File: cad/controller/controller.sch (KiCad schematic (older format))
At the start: 64 parts, among them J1 RJ45_jack_POE, J2 Barrel_Jack, SW1 SW_Push, U1 NCP1117-5.0_SOT223, U2 NCP1117-3.3_SOT223, U3 CAT811STBI-GT3, U4 W5500, Y1 25MHz

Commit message: controller placement in progress
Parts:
- Y1: footprint Crystal:Crystal_SMD_HC49-SD_HandSoldering -> Crystal:Crystal_SMD_HC49-SD
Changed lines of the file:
@@
 F 0 "Y1" V 2404 4181 50  0000 L CNN
 F 1 "25MHz" V 2495 4181 50  0000 L CNN
-F 2 "Crystal:Crystal_SMD_HC49-SD_HandSoldering" H 2450 4050 50  0001 C CNN
+F 2 "Crystal:Crystal_SMD_HC49-SD" H 2450 4050 50  0001 C CNN
 F 3 "~" H 2450 4050 50  0001 C CNN
 	1    2450 4050

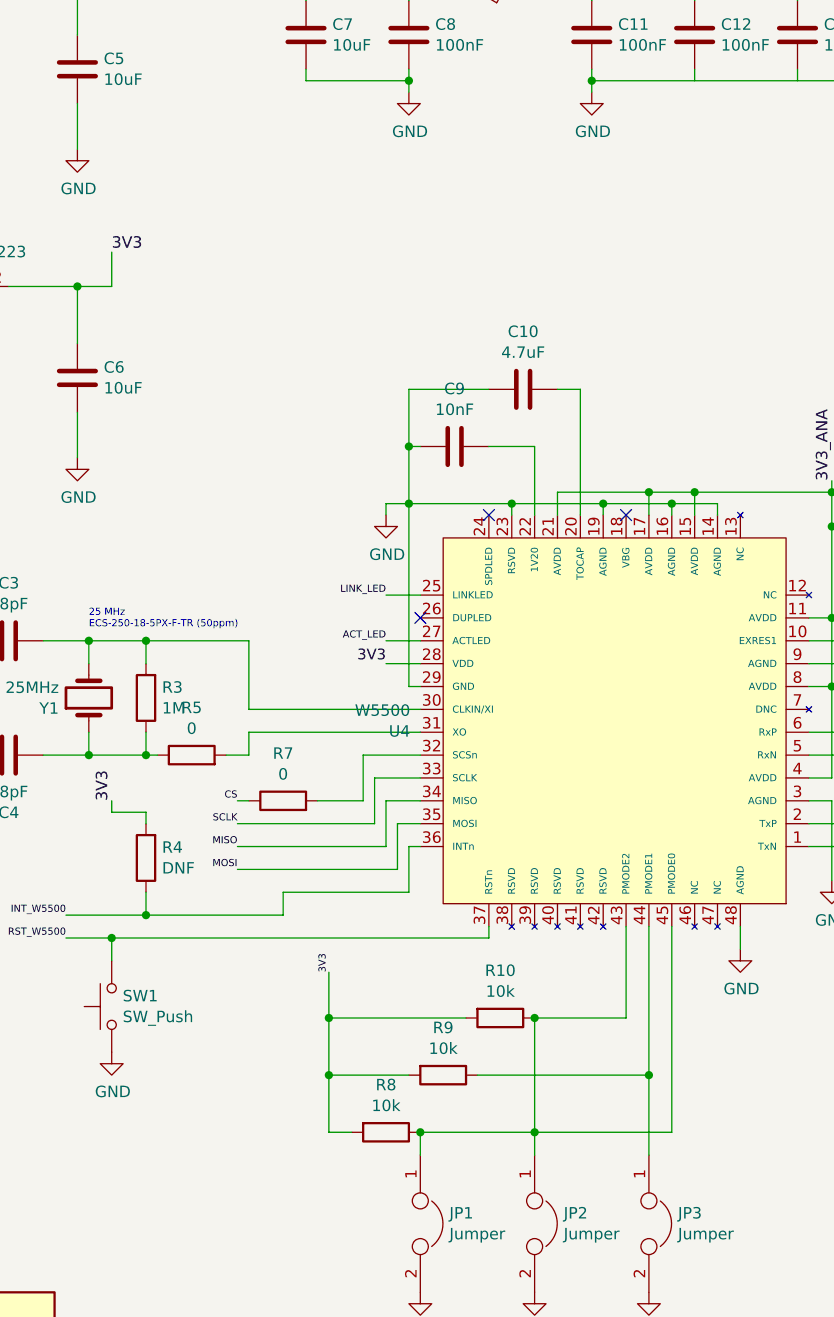
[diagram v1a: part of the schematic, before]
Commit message: Continued controller board placement
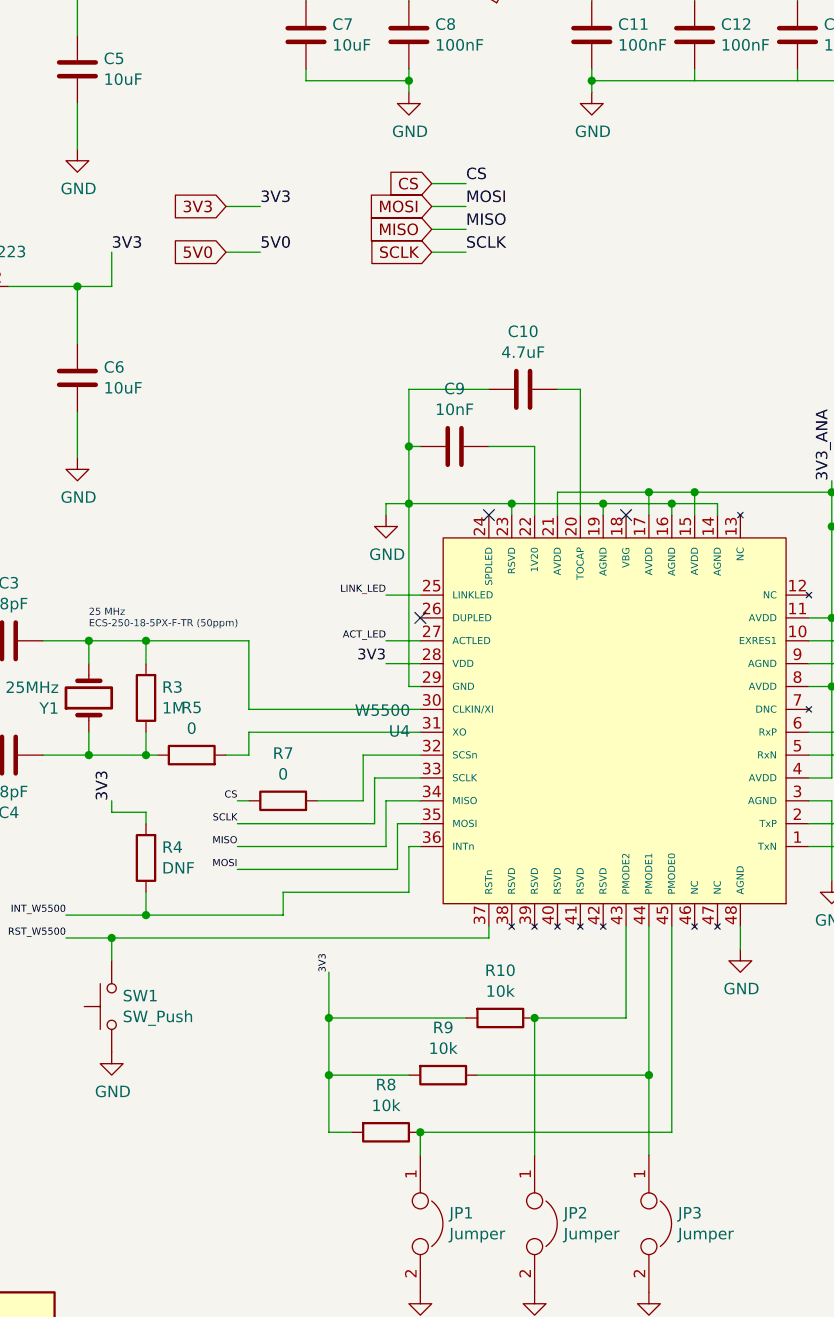
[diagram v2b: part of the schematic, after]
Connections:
- net at JP2.1, R10.1, U4.43 (PMODE2): no longer JP1.1, R8.1, U4.45 (PMODE0)
- new net: JP1.1, R8.1, U4.45 (PMODE0)
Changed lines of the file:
@@
 	2550 2250 2550 2100
 Connection ~ 2400 2250
-Text Label 2550 2100 0    50   ~ 0
-3V3
 $Comp
 L power:GND #PWR04
@@
 Wire Wire Line
 	4650 900  4650 1000
-Text Label 3250 900  2    50   ~ 0
-3V3
 Wire Wire Line
 	4400 900  4650 900
@@
 $EndComp
 Wire Wire Line
-	3900 5950 4400 5950
-Wire Wire Line
 	3900 6050 3900 5950
 Connection ~ 3900 5950
@@
 Wire Wire Line
 	4400 5450 4800 5450
-Wire Wire Line
-	4400 5950 4400 5450
-Connection ~ 4400 5450
 Wire Wire Line
 	7300 4350 7300 4750
@@
 Wire Wire Line
 	4900 5700 4900 6050
-Connection ~ 4400 5950
-Wire Wire Line
-	4400 5950 5000 5950
 Wire Wire Line
 	4800 5450 4800 5050
-Wire Wire Line
-	4400 6050 4400 5950
 Wire Wire Line
 	3500 5450 3500 5700
@@
 Wire Wire Line
 	9100 6100 8950 6100
+Wire Wire Line
+	3900 5950 5000 5950
+Wire Wire Line
+	4400 5450 4400 6050
+Connection ~ 4400 5450
+Text Label 3250 900  2    50   ~ 0
+3V3
+Text GLabel 3050 1900 0    50   Input ~ 0
+3V3
+Text Label 2550 2100 0    50   ~ 0
+3V3
+Text Label 3200 1900 0    50   ~ 0
+3V3
+Wire Wire Line
+	3050 1900 3200 1900
+Text GLabel 3050 2100 0    50   Input ~ 0
+5V0
+Text Label 3200 2100 0    50   ~ 0
+5V0
+Wire Wire Line
+	3050 2100 3200 2100
+Text Label 4100 2100 0    50   ~ 0
+SCLK
+Text Label 4100 2000 0    50   ~ 0
+MISO
+Text Label 4100 1900 0    50   ~ 0
+MOSI
+Text Label 4100 1800 0    50   ~ 0
+CS
+Text GLabel 3950 1800 0    50   Input ~ 0
+CS
+Text GLabel 3950 1900 0    50   Input ~ 0
+MOSI
+Text GLabel 3950 2000 0    50   Input ~ 0
+MISO
+Text GLabel 3950 2100 0    50   Input ~ 0
+SCLK
+Wire Wire Line
+	3950 1800 4100 1800
+Wire Wire Line
+	3950 1900 4100 1900
+Wire Wire Line
+	3950 2000 4100 2000
+Wire Wire Line
+	3950 2100 4100 2100
 $EndSCHEMATC

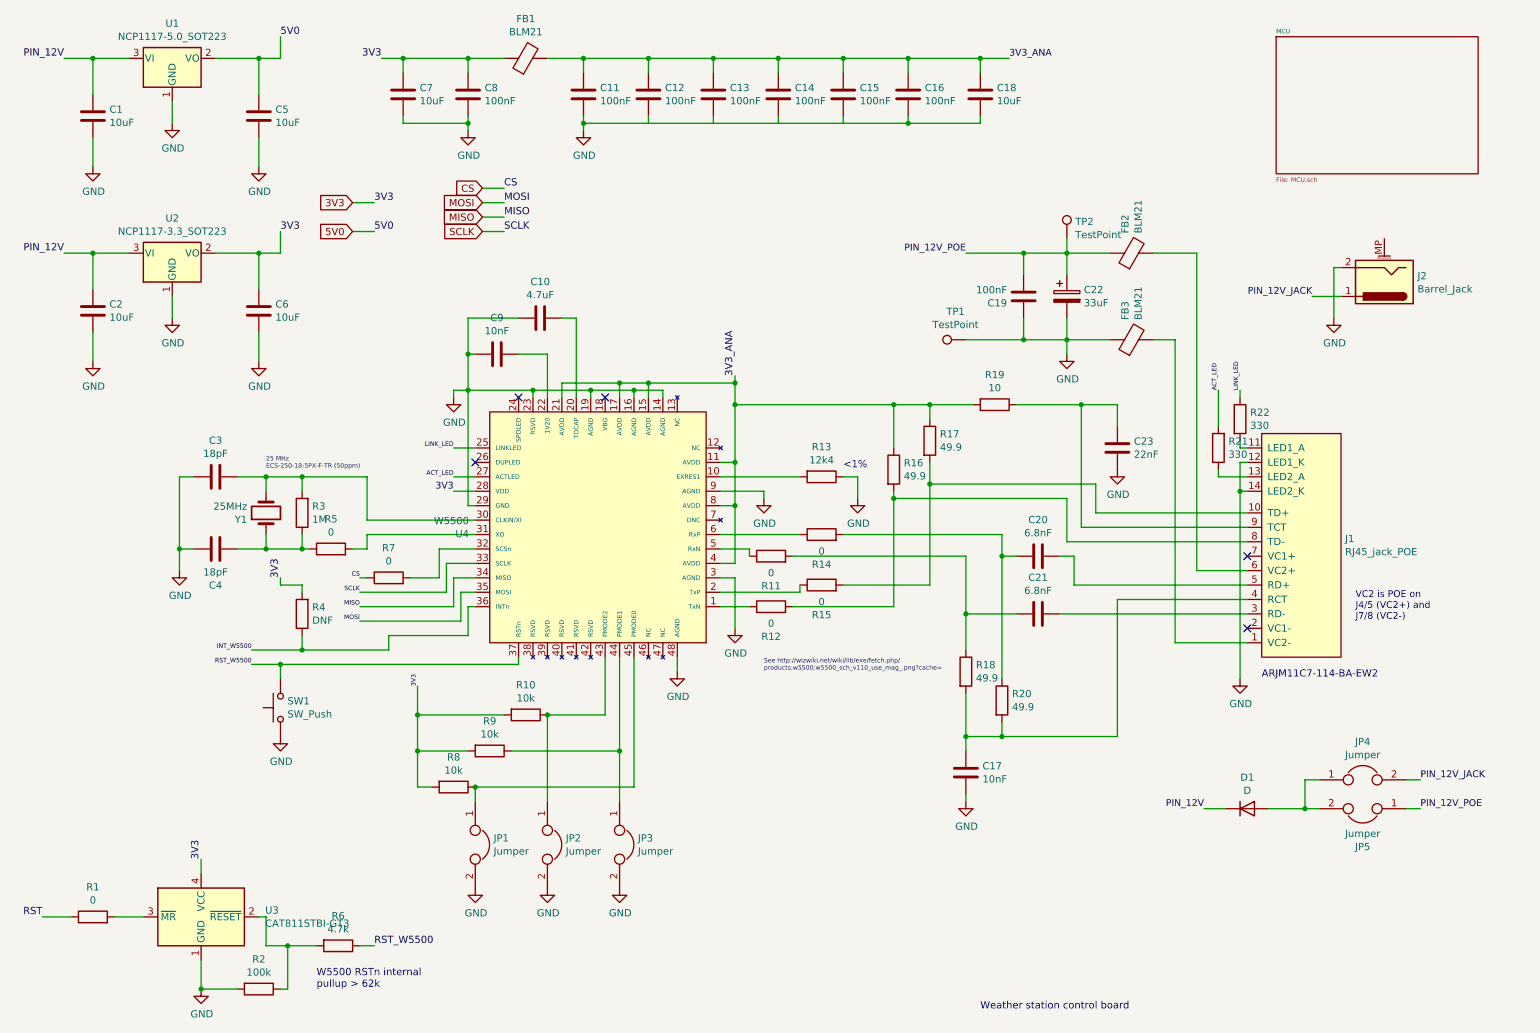
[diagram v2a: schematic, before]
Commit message: Finished placement of controller
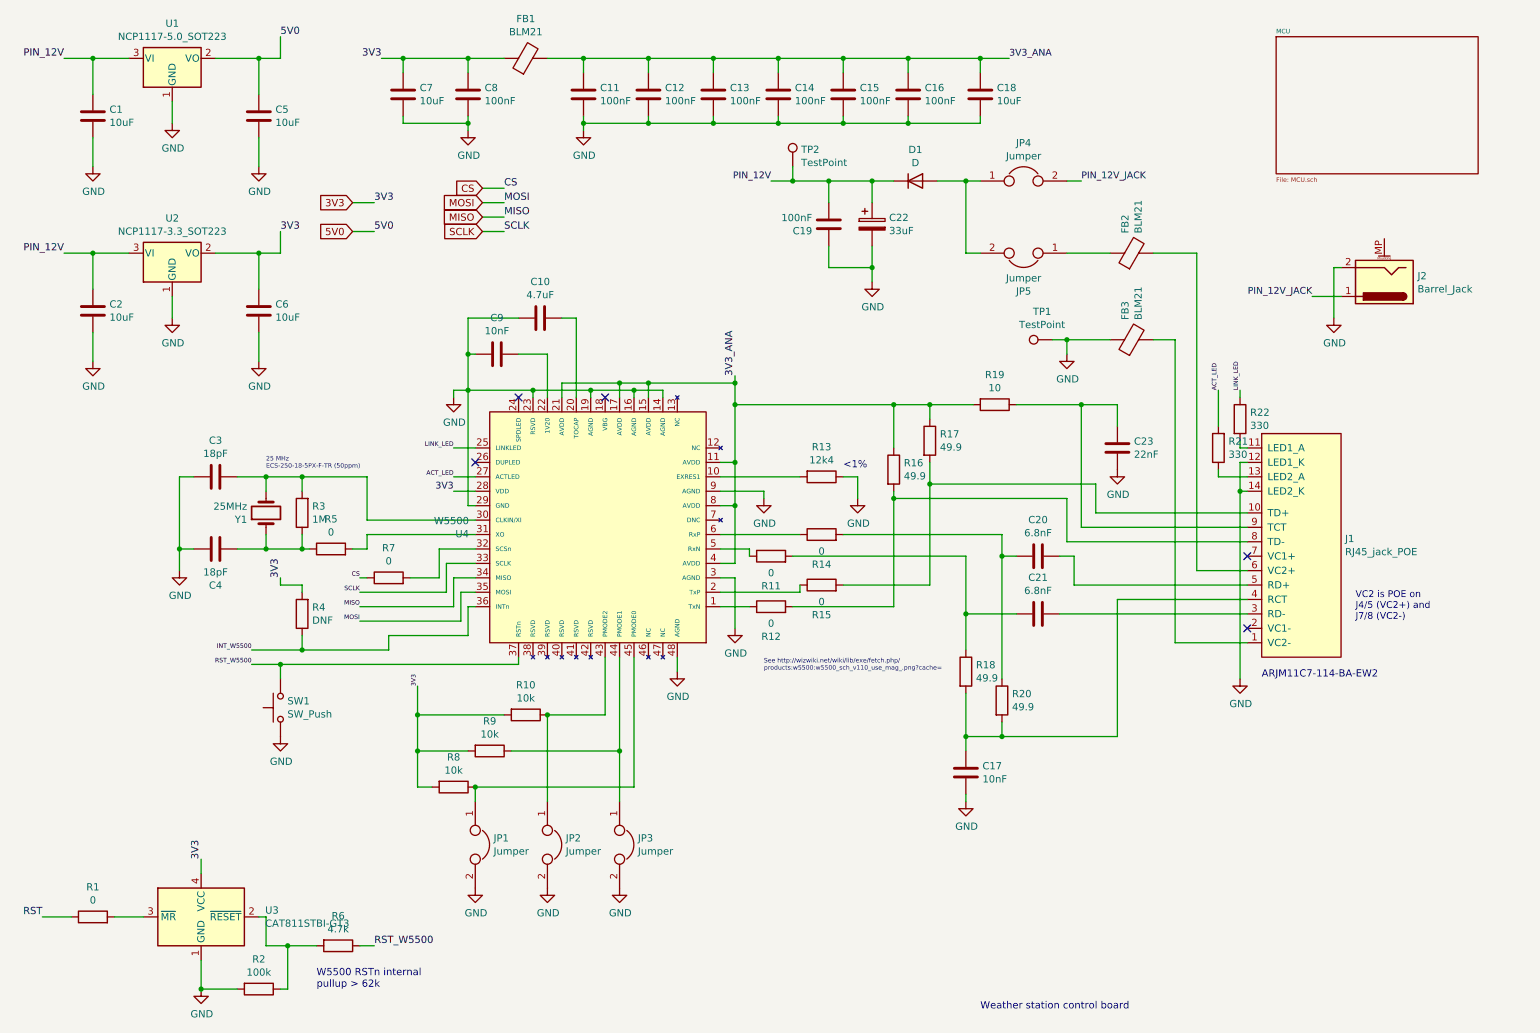
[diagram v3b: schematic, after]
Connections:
- net GND: now also C12.1, C13.1, C14.1, C15.1
- net PIN_12V: now also C19.1, C22.1, TP2.1
- removed net PIN_12V_POE: C19.1, C22.1, FB2.1, JP5.1, TP2.1
- new net: FB2.1, JP5.1
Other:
- moved on the sheet: C19, C22, D1, JP4, JP5, TP1, TP2
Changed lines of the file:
@@
 Text Notes 10000 4800 0    47   ~ 0
 VC2 is POE on\nJ4/5 (VC2+) and\nJ7/8 (VC2-)
-Text Label 7300 2250 2    47   ~ 0
-PIN_12V_POE
 NoConn ~ 9250 4350
 NoConn ~ 9250 4850
@@
 L Device:Jumper JP5
 U 1 1 624A0154
-P 10050 6100
-F 0 "JP5" H 10050 6364 50  0000 C CNN
-F 1 "Jumper" H 10050 6273 50  0000 C CNN
-F 2 "Connector_PinSocket_2.54mm:PinSocket_1x02_P2.54mm_Vertical" H 10050 6100 50  0001 C CNN
-F 3 "~" H 10050 6100 50  0001 C CNN
-	1    10050 6100
+P 7700 2250
+F 0 "JP5" H 7700 2514 50  0000 C CNN
+F 1 "Jumper" H 7700 2423 50  0000 C CNN
+F 2 "Connector_PinSocket_2.54mm:PinSocket_1x02_P2.54mm_Vertical" H 7700 2250 50  0001 C CNN
+F 3 "~" H 7700 2250 50  0001 C CNN
+	1    7700 2250
 	-1   0    0    1
 $EndComp
@@
 L Device:Jumper JP4
 U 1 1 624A141E
-P 10050 5900
-F 0 "JP4" H 10050 6164 50  0000 C CNN
-F 1 "Jumper" H 10050 6073 50  0000 C CNN
-F 2 "Connector_PinSocket_2.54mm:PinSocket_1x02_P2.54mm_Vertical" H 10050 5900 50  0001 C CNN
-F 3 "~" H 10050 5900 50  0001 C CNN
-	1    10050 5900
-	1    0    0    -1
-$EndComp
-Wire Wire Line
-	9750 5900 9650 5900
-Wire Wire Line
-	9650 5900 9650 6100
-Wire Wire Line
-	9750 6100 9650 6100
-Connection ~ 9650 6100
-Wire Wire Line
-	10350 6100 10450 6100
-Wire Wire Line
-	10350 5900 10450 5900
-Text Label 10450 6100 0    47   ~ 0
-PIN_12V_POE
-Text Label 10450 5900 0    47   ~ 0
+P 7700 1750
+F 0 "JP4" H 7700 2014 50  0000 C CNN
+F 1 "Jumper" H 7700 1923 50  0000 C CNN
+F 2 "Connector_PinSocket_2.54mm:PinSocket_1x02_P2.54mm_Vertical" H 7700 1750 50  0001 C CNN
+F 3 "~" H 7700 1750 50  0001 C CNN
+	1    7700 1750
+	1    0    0    -1
+$EndComp
+Wire Wire Line
+	7400 2250 7300 2250
+Wire Wire Line
+	8000 1750 8100 1750
+Text Label 8100 1750 0    47   ~ 0
 PIN_12V_JACK
-Text Label 8950 6100 2    47   ~ 0
+Text Label 5950 1750 2    47   ~ 0
 PIN_12V
 Wire Wire Line
@@
 Wire Wire Line
 	8600 2850 8750 2850
-Wire Wire Line
-	8000 2250 8300 2250
 $Comp
 L power:GND #PWR021
@@
 	1    0    0    -1
 $EndComp
-Connection ~ 8000 2250
 Wire Wire Line
 	8000 2850 8000 2950
-Connection ~ 8000 2850
 $Comp
 L Connector:TestPoint TP2
 U 1 1 62BD0C2D
-P 8000 2150
-F 0 "TP2" H 8058 2268 50  0000 L CNN
-F 1 "TestPoint" H 8058 2177 50  0000 L CNN
-F 2 "TestPoint:TestPoint_Pad_2.5x2.5mm" H 8200 2150 50  0001 C CNN
-F 3 "~" H 8200 2150 50  0001 C CNN
-	1    8000 2150
-	1    0    0    -1
-$EndComp
-$Comp
-L Connector:TestPoint TP1
-U 1 1 62BD24C9
-P 7300 2850
-F 0 "TP1" V 7495 2922 50  0000 C CNN
-F 1 "TestPoint" V 7404 2922 50  0000 C CNN
-F 2 "TestPoint:TestPoint_Pad_2.5x2.5mm" H 7500 2850 50  0001 C CNN
-F 3 "~" H 7500 2850 50  0001 C CNN
-	1    7300 2850
-	0    -1   -1   0
+P 6100 1650
+F 0 "TP2" H 6158 1768 50  0000 L CNN
+F 1 "TestPoint" H 6158 1677 50  0000 L CNN
+F 2 "TestPoint:TestPoint_Pad_2.5x2.5mm" H 6300 1650 50  0001 C CNN
+F 3 "~" H 6300 1650 50  0001 C CNN
+	1    6100 1650
+	1    0    0    -1
 $EndComp
 Wire Wire Line
 	8300 2850 8000 2850
-Wire Wire Line
-	8000 2250 8000 2150
 $Comp
 L Device:C C8
@@
 Wire Wire Line
 	3850 900  3850 1000
-Wire Wire Line
-	4650 1300 4650 1350
-Wire Wire Line
-	4650 1350 6900 1350
 $Comp
 L Device:C C12
@@
 	-1   0    0    1
 $EndComp
-Wire Wire Line
-	5100 1300 5100 1350
 $Comp
 L Device:C C13
@@
 	-1   0    0    1
 $EndComp
-Wire Wire Line
-	5550 1300 5550 1350
 $Comp
 L Device:C C14
@@
 	-1   0    0    1
 $EndComp
-Wire Wire Line
-	6000 1300 6000 1350
 $Comp
 L Device:C C15
@@
 	-1   0    0    1
 $EndComp
-Wire Wire Line
-	6450 1300 6450 1350
 $Comp
 L Device:C C16
@@
 Wire Wire Line
 	6900 1350 7400 1350
-Connection ~ 6900 1350
-Wire Wire Line
-	4650 1350 4650 1400
-Connection ~ 4650 1350
 Connection ~ 3850 1350
 $Comp
 L Device:CP C22
 U 1 1 6313C837
-P 8000 2550
-F 0 "C22" H 8118 2596 50  0000 L CNN
-F 1 "33uF" H 8118 2505 50  0000 L CNN
-F 2 "Capacitor_THT:CP_Radial_D4.0mm_P2.00mm" H 8038 2400 50  0001 C CNN
-F 3 "~" H 8000 2550 50  0001 C CNN
-	1    8000 2550
-	1    0    0    -1
-$EndComp
-Wire Wire Line
-	8000 2250 8000 2400
-Wire Wire Line
-	8000 2700 8000 2850
+P 6650 2050
+F 0 "C22" H 6768 2096 50  0000 L CNN
+F 1 "33uF" H 6768 2005 50  0000 L CNN
+F 2 "Capacitor_THT:CP_Radial_D4.0mm_P2.00mm" H 6688 1900 50  0001 C CNN
+F 3 "~" H 6650 2050 50  0001 C CNN
+	1    6650 2050
+	1    0    0    -1
+$EndComp
+Wire Wire Line
+	6650 1750 6650 1900
+Wire Wire Line
+	6650 2200 6650 2350
 $Comp
 L Device:C C19
 U 1 1 62415D4C
-P 7700 2550
-F 0 "C19" H 7585 2504 50  0000 R CNN
-F 1 "100nF" H 7585 2595 50  0000 R CNN
-F 2 "Capacitor_SMD:C_0603_1608Metric" H 7738 2400 50  0001 C CNN
-F 3 "~" H 7700 2550 50  0001 C CNN
-	1    7700 2550
-	1    0    0    -1
-$EndComp
-Wire Wire Line
-	7700 2250 7700 2400
-Wire Wire Line
-	7700 2250 8000 2250
-Wire Wire Line
-	7700 2850 7700 2700
-Wire Wire Line
-	7700 2850 8000 2850
-Wire Wire Line
-	7700 2850 7300 2850
-Connection ~ 7700 2850
-Wire Wire Line
-	7700 2250 7300 2250
-Connection ~ 7700 2250
+P 6350 2050
+F 0 "C19" H 6235 2004 50  0000 R CNN
+F 1 "100nF" H 6235 2095 50  0000 R CNN
+F 2 "Capacitor_SMD:C_0603_1608Metric" H 6388 1900 50  0001 C CNN
+F 3 "~" H 6350 2050 50  0001 C CNN
+	1    6350 2050
+	1    0    0    -1
+$EndComp
+Wire Wire Line
+	6350 1750 6350 1900
+Wire Wire Line
+	6350 2350 6350 2200
 $Comp
 L Device:C C7
@@
 L Device:D D1
 U 1 1 62437589
-P 9250 6100
-F 0 "D1" H 9250 6317 50  0000 C CNN
-F 1 "D" H 9250 6226 50  0000 C CNN
-F 2 "Diode_THT:D_DO-41_SOD81_P7.62mm_Horizontal" H 9250 6100 50  0001 C CNN
-F 3 "~" H 9250 6100 50  0001 C CNN
-	1    9250 6100
-	1    0    0    -1
-$EndComp
-Wire Wire Line
-	9400 6100 9650 6100
-Wire Wire Line
-	9100 6100 8950 6100
+P 6950 1750
+F 0 "D1" H 6950 1967 50  0000 C CNN
+F 1 "D" H 6950 1876 50  0000 C CNN
+F 2 "Diode_THT:D_DO-41_SOD81_P7.62mm_Horizontal" H 6950 1750 50  0001 C CNN
+F 3 "~" H 6950 1750 50  0001 C CNN
+	1    6950 1750
+	1    0    0    -1
+$EndComp
+Wire Wire Line
+	6800 1750 6650 1750
 Wire Wire Line
 	3900 5950 5000 5950
@@
 Wire Wire Line
 	3950 2100 4100 2100
+Wire Wire Line
+	4650 1300 4650 1350
+Wire Wire Line
+	6450 1300 6450 1350
+Wire Wire Line
+	6450 1350 6900 1350
+Connection ~ 6900 1350
+Wire Wire Line
+	6000 1300 6000 1350
+Wire Wire Line
+	6000 1350 6450 1350
+Connection ~ 6450 1350
+Wire Wire Line
+	5550 1300 5550 1350
+Wire Wire Line
+	5550 1350 6000 1350
+Connection ~ 6000 1350
+Wire Wire Line
+	5100 1300 5100 1350
+Wire Wire Line
+	5100 1350 5550 1350
+Connection ~ 5550 1350
+Wire Wire Line
+	5100 1350 4650 1350
+Connection ~ 5100 1350
+Connection ~ 4650 1350
+Wire Wire Line
+	4650 1350 4650 1400
+Wire Wire Line
+	7100 1750 7300 1750
+$Comp
+L Connector:TestPoint TP1
+U 1 1 62BD24C9
+P 7900 2850
+F 0 "TP1" V 8095 2922 50  0000 C CNN
+F 1 "TestPoint" V 8004 2922 50  0000 C CNN
+F 2 "TestPoint:TestPoint_Pad_2.5x2.5mm" H 8100 2850 50  0001 C CNN
+F 3 "~" H 8100 2850 50  0001 C CNN
+	1    7900 2850
+	0    -1   -1   0
+$EndComp
+Wire Wire Line
+	8000 2850 7900 2850
+Connection ~ 8000 2850
+Wire Wire Line
+	7300 1750 7400 1750
+Wire Wire Line
+	8000 2250 8300 2250
+Connection ~ 7300 1750
+Wire Wire Line
+	7300 1750 7300 2250
+Wire Wire Line
+	6350 1750 6650 1750
+Connection ~ 6650 1750
+Wire Wire Line
+	6350 1750 6100 1750
+Wire Wire Line
+	6100 1750 6100 1650
+Connection ~ 6350 1750
+Wire Wire Line
+	6100 1750 5950 1750
+Connection ~ 6100 1750
+Wire Wire Line
+	6350 2350 6650 2350
+Wire Wire Line
+	6650 2350 6650 2450
+Connection ~ 6650 2350
+$Comp
+L power:GND #PWR0101
+U 1 1 62D48985
+P 6650 2450
+F 0 "#PWR0101" H 6650 2200 50  0001 C CNN
+F 1 "GND" H 6655 2277 50  0000 C CNN
+F 2 "" H 6650 2450 50  0001 C CNN
+F 3 "" H 6650 2450 50  0001 C CNN
+	1    6650 2450
+	1    0    0    -1
+$EndComp
 $EndSCHEMATC

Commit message: Began routing controller
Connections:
- net at FB3.2, J1.1 (VC2-): now also J1.2 (VC1-)
- net at FB2.2, J1.6 (VC2+): now also J1.7 (VC1+)
- no-connect marks 5 -> 3
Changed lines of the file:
@@
 Text Notes 10000 4800 0    47   ~ 0
 VC2 is POE on\nJ4/5 (VC2+) and\nJ7/8 (VC2-)
-NoConn ~ 9250 4350
-NoConn ~ 9250 4850
 $Comp
 L Device:Jumper JP5
@@
 	8100 3300 8100 4150
 Wire Wire Line
-	8900 4450 9250 4450
+	8900 4450 9100 4450
 Wire Wire Line
 	8050 4550 9250 4550
@@
 $EndComp
 Wire Wire Line
-	8750 4950 9250 4950
-Wire Wire Line
-	9200 3900 9200 5200
-Connection ~ 9200 3900
+	8750 4950 9100 4950
 $Comp
 L power:GND #PWR023
@@
 	1    0    0    -1
 $EndComp
+Connection ~ 9200 3900
+Wire Wire Line
+	9200 3900 9200 5200
+Wire Wire Line
+	9250 4850 9100 4850
+Wire Wire Line
+	9100 4850 9100 4950
+Connection ~ 9100 4950
+Wire Wire Line
+	9100 4950 9250 4950
+Wire Wire Line
+	9250 4350 9100 4350
+Wire Wire Line
+	9100 4350 9100 4450
+Connection ~ 9100 4450
+Wire Wire Line
+	9100 4450 9250 4450
 $EndSCHEMATC
